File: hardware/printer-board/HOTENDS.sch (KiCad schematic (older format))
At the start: 0 parts

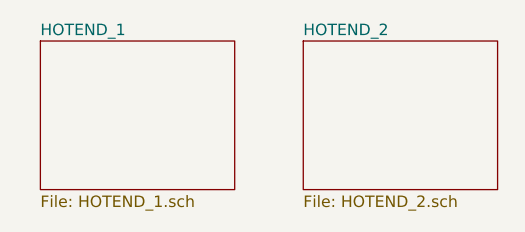
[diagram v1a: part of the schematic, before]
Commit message: update power supply circuit,
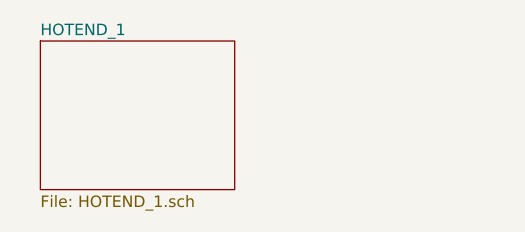
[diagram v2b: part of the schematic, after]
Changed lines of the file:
@@
 $Descr A4 11693 8268
 encoding utf-8
-Sheet 26 33
+Sheet 24 32
 Title ""
 Date ""
@@
 F1 "HOTEND_1.sch" 50
 $EndSheet
-$Sheet
-S 5050 3200 850  650
-U 5CC222D5
-F0 "HOTEND_2" 50
-F1 "HOTEND_2.sch" 50
-$EndSheet
 $EndSCHEMATC

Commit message: update,
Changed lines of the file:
@@
 F0 "HOTEND_0" 50
 F1 "HOTEND_0.sch" 50
+F2 "EN1" I L 2750 3450 50
 $EndSheet
 $Sheet
-S 3900 3200 850  650
+S 5600 3200 850  650
 U 5CC222D3
 F0 "HOTEND_1" 50
 F1 "HOTEND_1.sch" 50
+F2 "EN2" I L 5600 3450 50
 $EndSheet
+Text HLabel 1450 750  0    50   Input ~ 0
+HOTEND_EN1
+Text HLabel 1450 850  0    50   Input ~ 0
+HOTEND_EN2
+Text Label 2150 750  2    50   ~ 0
+EN1
+Text Label 2150 850  2    50   ~ 0
+EN2
+Wire Wire Line
+	2150 750  1450 750
+Wire Wire Line
+	2150 850  1450 850
+Text Label 2050 3450 0    50   ~ 0
+EN1
+Text Label 4900 3450 0    50   ~ 0
+EN2
+Wire Wire Line
+	2050 3450 2750 3450
+Wire Wire Line
+	4900 3450 5600 3450
 $EndSCHEMATC
